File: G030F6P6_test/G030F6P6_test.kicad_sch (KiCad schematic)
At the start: 1 part

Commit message: Update G030F6P6_test.kicad_sch
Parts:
- added J?: Conn_01x10_Female, Connector_PinHeader_2.54mm:PinHeader_1x10_P2.54mm_Vertical, symbol Connector:Conn_01x10_Female
- added J?: (no value), symbol Connector:Conn_01x10_Female
- U?: value (none) -> STM32G030FxP; footprint (none) -> Package_SO:TSSOP-20_4.4x6.5mm_P0.65mm
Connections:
- net PIN1: now reaches U?.1 (PB7/PB8)
- net PIN1: now also J?.1 (Pin_1)
- net PIN10: now reaches U?.10 (PA3)
- net PIN10: now also J?.10 (Pin_10)
- net PIN11: now reaches U?.11 (PA4)
- net PIN11: now also J?.1 (Pin_1)
- net PIN12: now reaches U?.12 (PA5)
- net PIN12: now also J?.2 (Pin_2)
- net PIN13: now reaches U?.13 (PA6)
- net PIN13: now also J?.3 (Pin_3)
- net PIN14: now reaches U?.14 (PA7)
- net PIN14: now also J?.4 (Pin_4)
- net PIN15: now reaches U?.15 (PB0/PB1/PB2/PA8)
- net PIN15: now also J?.5 (Pin_5)
- net PIN16: now reaches U?.16 (PA11[PA9])
- net PIN16: now also J?.6 (Pin_6)
- net PIN17: now reaches U?.17 (PA12[PA10])
- net PIN17: now also J?.7 (Pin_7)
- net PIN18: now reaches U?.18 (PA13)
- net PIN18: now also J?.8 (Pin_8)
- net PIN19: now reaches U?.19 (PA15/PA14-BOOT0)
- net PIN19: now also J?.9 (Pin_9)
- net PIN2: now reaches U?.2 (PB9/PC14-OSC32_IN)
- net PIN2: now also J?.2 (Pin_2)
- net PIN20: now reaches U?.20 (PB3/PB4/PB5/PB6)
- net PIN20: now also J?.10 (Pin_10)
- net PIN3: now reaches U?.3 (PC15-OSC32_OUT)
- net PIN3: now also J?.3 (Pin_3)
- net PIN4: now reaches U?.4 (VDD/VDDA)
- net PIN4: now also J?.4 (Pin_4)
- net PIN5: now reaches U?.5 (VSS/VSSA)
- net PIN5: now also J?.5 (Pin_5)
- net PIN6: now reaches U?.6 (NRST)
- net PIN6: now also J?.6 (Pin_6)
- net PIN7: now reaches U?.7 (PA0)
- net PIN7: now also J?.7 (Pin_7)
- net PIN8: now reaches U?.8 (PA1)
- net PIN8: now also J?.8 (Pin_8)
- net PIN9: now reaches U?.9 (PA2)
- net PIN9: now also J?.9 (Pin_9)

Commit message: Update G030F6P6_test.kicad_sch
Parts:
- J1: renamed from J?; value (none) -> Conn_01x10_Female; footprint (none) -> Connector_PinHeader_2.54mm:PinHeader_1x10_P2.54mm_Vertical
- gave numbers to parts that had none: 2
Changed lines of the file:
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@@
   (symbol (lib_id "Connector:Conn_01x10_Female") (at 67.31 120.015 0) (unit 1)
     (in_bom yes) (on_board yes)
-    (property "Reference" "J?" (id 0) (at 63.5 106.045 0)
+    (property "Reference" "J2" (id 0) (at 63.5 106.045 0)
       (effects (font (size 1.27 1.27)) (justify left))
     )
@@
   (symbol (lib_id "MCU_ST_STM32G0:STM32G030FxP") (at 151.13 87.63 0) (unit 1)
     (in_bom yes) (on_board yes) (fields_autoplaced)
-    (property "Reference" "U?" (id 0) (at 139.065 66.04 0))
+    (property "Reference" "U1" (id 0) (at 139.065 66.04 0))
     (property "Value" "STM32G030FxP" (id 1) (at 139.065 68.58 0))
     (property "Footprint" "Package_SO:TSSOP-20_4.4x6.5mm_P0.65mm" (id 2) (at 181.61 121.92 0)
@@
   (symbol (lib_id "Connector:Conn_01x10_Female") (at 67.31 89.535 0) (unit 1)
     (in_bom yes) (on_board yes)
-    (property "Reference" "J?" (id 0) (at 63.5 75.565 0)
+    (property "Reference" "J1" (id 0) (at 63.5 75.565 0)
       (effects (font (size 1.27 1.27)) (justify left))
     )
-    (property "Value" "" (id 1) (at 69.215 92.0749 0)
+    (property "Value" "Conn_01x10_Female" (id 1) (at 69.215 92.0749 0)
       (effects (font (size 1.27 1.27)) (justify left) hide)
     )
-    (property "Footprint" "" (id 2) (at 67.31 89.535 0)
+    (property "Footprint" "Connector_PinHeader_2.54mm:PinHeader_1x10_P2.54mm_Vertical" (id 2) (at 67.31 89.535 0)
       (effects (font (size 1.27 1.27)) hide)
     )
@@
   )
   (symbol_instances
+    (path "/e9b753db-4772-4244-b88b-22e987cc4a07"
+      (reference "J1") (unit 1) (value "Conn_01x10_Female") (footprint "Connector_PinHeader_2.54mm:PinHeader_1x10_P2.54mm_Vertical")
+    )
     (path "/dea68bd7-448e-4645-961d-024e3f8df3a0"
-      (reference "J?") (unit 1) (value "Conn_01x10_Female") (footprint "Connector_PinHeader_2.54mm:PinHeader_1x10_P2.54mm_Vertical")
-    )
-    (path "/e9b753db-4772-4244-b88b-22e987cc4a07"
-      (reference "J?") (unit 1) (value "Conn_01x10_Female") (footprint "Connector_PinHeader_2.54mm:PinHeader_1x10_P2.54mm_Vertical")
+      (reference "J2") (unit 1) (value "Conn_01x10_Female") (footprint "Connector_PinHeader_2.54mm:PinHeader_1x10_P2.54mm_Vertical")
     )
     (path "/e65b62be-e01b-4688-a999-1d1be370c4ae"
-      (reference "U?") (unit 1) (value "STM32G030FxP") (footprint "Package_SO:TSSOP-20_4.4x6.5mm_P0.65mm")
+      (reference "U1") (unit 1) (value "STM32G030FxP") (footprint "Package_SO:TSSOP-20_4.4x6.5mm_P0.65mm")
     )
   )

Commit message: Update G030F6P6_test.kicad_sch
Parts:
- added C? (x4): 0.1uF, Capacitor_SMD:C_0805_2012Metric, symbol Device:C
- added D?: TX, LED_SMD:LED_0805_2012Metric, symbol Device:LED
- added D?: PWR, LED_SMD:LED_0805_2012Metric, symbol Device:LED
- added D?: RX, LED_SMD:LED_0805_2012Metric, symbol Device:LED
- added F?: Fuse, Fuse:Fuse_0805_2012Metric, symbol Device:Fuse
- added J?: USB_C_Receptacle_USB2.0, Connector_USB:USB_C_Receptacle_HRO_TYPE-C-31-M-12, symbol Connector:USB_C_Receptacle_USB2.0
- added JP? (x2): SolderJumper_2_Bridged, Jumper:SolderJumper-2_P1.3mm_Bridged2Bar_RoundedPad1.0x1.5mm, symbol Jumper:SolderJumper_2_Bridged
- added JP?: (no value), symbol Jumper:SolderJumper_2_Bridged
- added R? (x2): 1k, Resistor_SMD:R_0805_2012Metric, symbol Device:R
- added R?: 330, Resistor_SMD:R_0805_2012Metric, symbol Device:R
- added R? (x2): 5K1, Resistor_SMD:R_0805_2012Metric, symbol Device:R
- added U?: XC6206P332MR, Package_TO_SOT_SMD:SOT-23, symbol Regulator_Linear:XC6206PxxxMR
- added U?: CH340N, Package_SO:SOIC-8_3.9x4.9mm_P1.27mm, symbol Interface_USB:CH330N
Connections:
- new net: F?.1, J?.A4 (VBUS), J?.A9 (VBUS), J?.B4 (VBUS), J?.B9 (VBUS)
- new net: D?.2 (A), R?.1 (x3)
- new net +3V3: C?.1, U?.2 (VO)
- new net +5V: C?.1, F?.2, U?.3 (VI)
- new net 3V3: C?.1, U?.8 (V3)
- new net CC1: J?.A5 (CC1), R?.2
- new net CC2: J?.B5 (CC2), R?.2
- new net GND: C?.2, C?.2, C?.2, C?.2, D?.1 (K), J?.A1 (GND), J?.A12 (GND), J?.B1 (GND), J?.B12 (GND), J?.S1 (SHIELD), R?.1, R?.1, U?.1 (GND), U?.3 (GND)
- new net RXD: D?.1 (K), U?.7 (RXD)
- new net TXD: D?.1 (K), U?.6 (TXD)
- new net USBD+: J?.A6 (D+), J?.B6 (D+), U?.1 (UD+)
- new net USBD-: J?.A7 (D-), J?.B7 (D-), U?.2 (UD-)
- new net VCC: C?.1, R?.2, R?.2, R?.2, U?.5 (VCC)
- new net ~{RTS}: U?.4 (~{RTS})
- no-connect marks 0 -> 2
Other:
- note added: "CH340N USB-UART chip"
- note added: "LED"
- note added: "USB TYPE-C & Fuse"
- note added: "voltage regulator"
- moved on the sheet: J1, J2, U1

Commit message: add 元件
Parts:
- added J?: Conn_01x05_Female, Connector_PinHeader_2.54mm:PinHeader_1x05_P2.54mm_Vertical, symbol Connector:Conn_01x05_Female
- added JP? (x3): SolderJumper_2_Bridged, Jumper:SolderJumper-2_P1.3mm_Bridged2Bar_RoundedPad1.0x1.5mm, symbol Jumper:SolderJumper_2_Bridged
- added R?: (no value), symbol Device:R
- JP?: value (none) -> SolderJumper_2_Bridged; footprint (none) -> Jumper:SolderJumper-2_P1.3mm_Bridged2Bar_RoundedPad1.0x1.5mm
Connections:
- net +3V3: now also J?.1 (Pin_1)
- net GND: now also J?.2 (Pin_2), R?.1
- net PIN1: now also JP?.2 (B)
- net PIN19: now also JP?.2 (B), R?.2
- net PIN20: now also JP?.2 (B)
- net RXD: now also JP?.1 (A)
- net TXD: now also JP?.1 (A)
- net ~{RTS}: now also JP?.1 (A)
- new net NRST: J?.5 (Pin_5)
- new net SWCLK: J?.4 (Pin_4)
- new net SWDIO: J?.3 (Pin_3)
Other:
- note added: "SWD connect"
- moved on the sheet: JP?

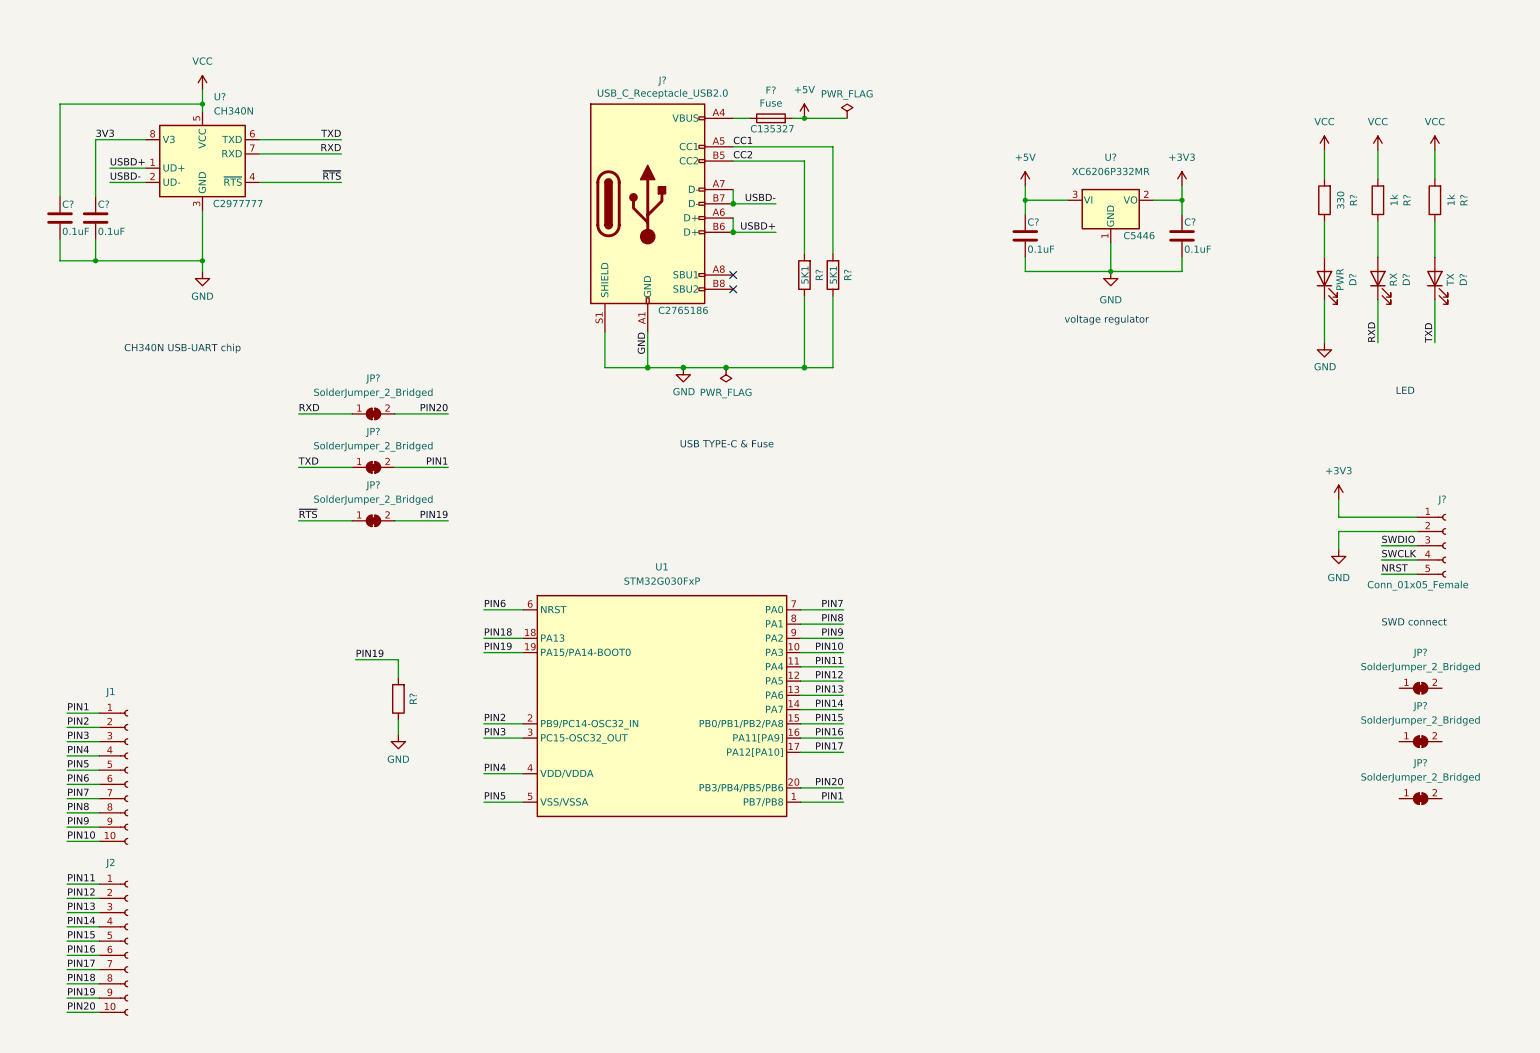
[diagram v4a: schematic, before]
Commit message: Update G030F6P6_test.kicad_sch
移除jump 的 BOM 標記
新增CH343P 元件
連結各對外腳位(SWD、UART、BOOT0)
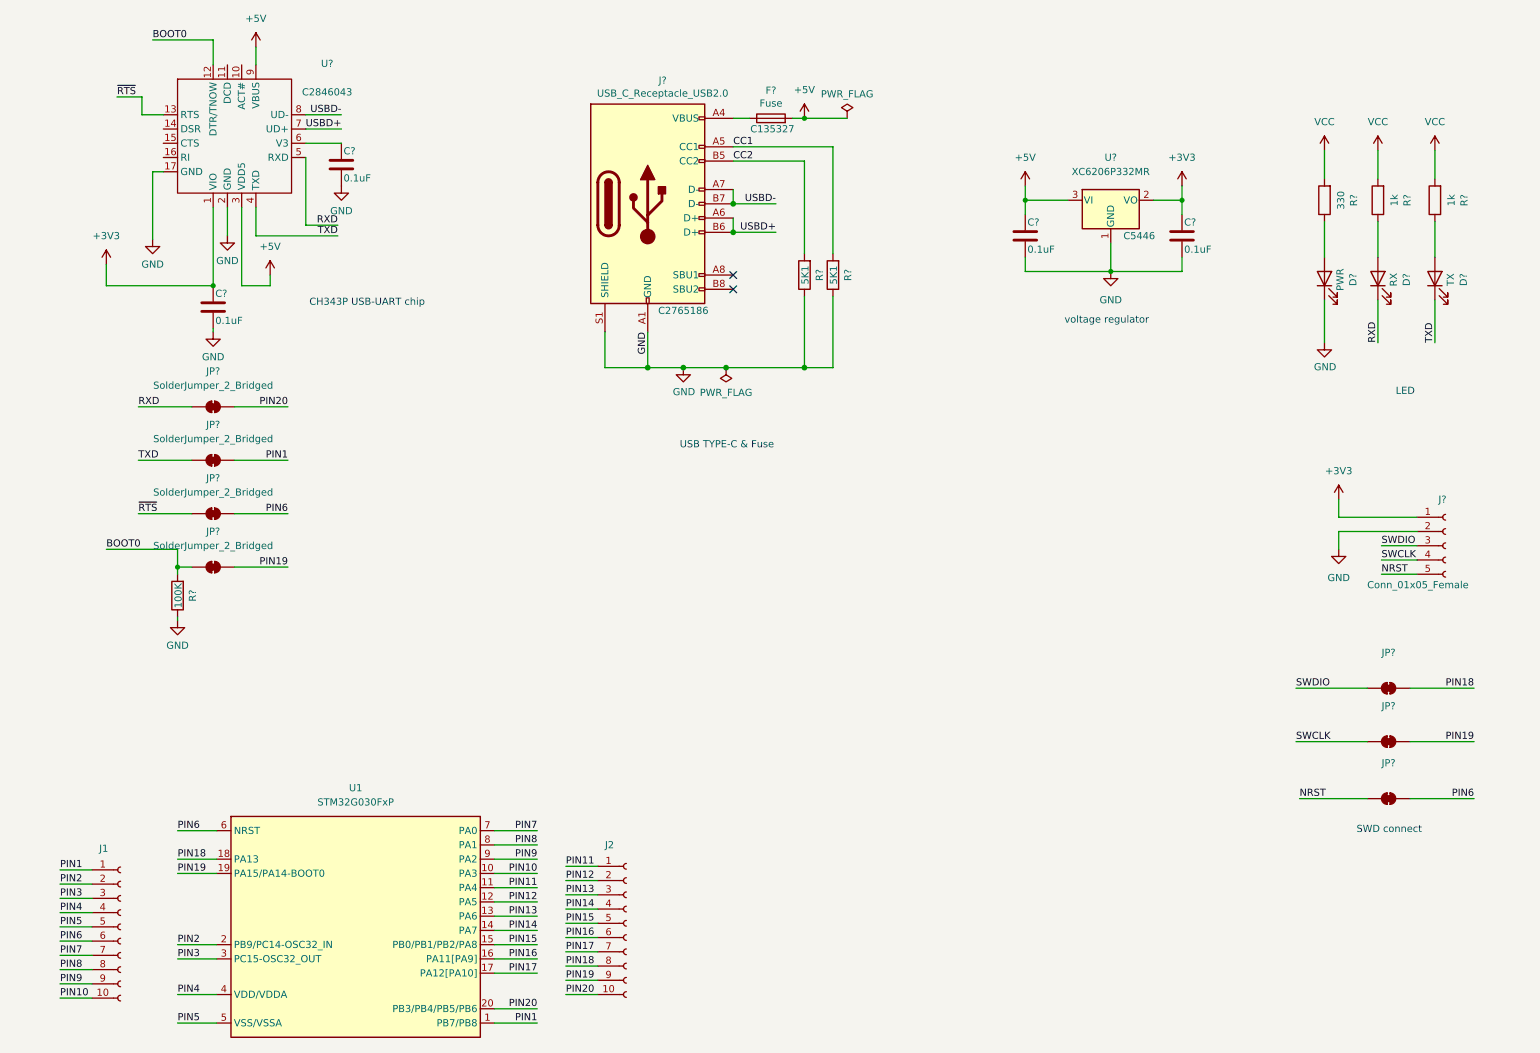
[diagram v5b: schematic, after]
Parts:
- removed JP? (x3): SolderJumper_2_Bridged, Jumper:SolderJumper-2_P1.3mm_Bridged2Bar_RoundedPad1.0x1.5mm, symbol Jumper:SolderJumper_2_Bridged
- removed U?: CH340N, Package_SO:SOIC-8_3.9x4.9mm_P1.27mm, symbol Interface_USB:CH330N
- added JP? (x4): SolderJumper_2_Bridged, Jumper:SolderJumper-2_P1.3mm_Bridged2Bar_RoundedPad1.0x1.5mm, symbol Jumper:SolderJumper_2_Bridged
- added U?: (no value), symbol Interface_USB:CH343P
- JP? (x3): value SolderJumper_2_Bridged -> (none); footprint Jumper:SolderJumper-2_P1.3mm_Bridged2Bar_RoundedPad1.0x1.5mm -> (none); now left out of the parts list
- R?: value (none) -> 100K; footprint (none) -> Resistor_SMD:R_0805_2012Metric
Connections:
- net +3V3: now also C?.1, U?.1 (VIO)
- net +5V: now also U?.3 (VDD5), U?.9 (VBUS)
- net GND: now also U?.17 (GND), U?.2 (GND)
- net NRST: now also JP?.1 (A)
- net PIN1: now also JP?.2 (B)
- net PIN18: now also JP?.2 (B)
- net PIN19: now also JP?.2 (B), JP?.2 (B); no longer R?.2
- net PIN20: now also JP?.2 (B)
- net PIN6: now also JP?.2 (B), JP?.2 (B)
- net RXD: now also JP?.1 (A), U?.5 (RXD)
- net SWCLK: now also JP?.1 (A)
- net SWDIO: now also JP?.1 (A)
- net TXD: now also JP?.1 (A), U?.4 (TXD)
- net USBD+: now also U?.7 (UD+)
- net USBD-: now also U?.8 (UD-)
- net VCC: no longer C?.1
- net ~{RTS}: now also JP?.1 (A), U?.13 (RTS)
- net 3V3: no longer names the net of C?.1
- net 3V3: now also U?.6 (V3)
- new net BOOT0: JP?.1 (A), R?.2, U?.12 (DTR/TNOW)
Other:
- note added: "CH343P USB-UART chip"
- note removed: "CH340N USB-UART chip"
- moved on the sheet: C?, J1, J2, R?, U1

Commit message: Update G030F6P6_test.kicad_sch
增加 VBUS、外部電源選擇接腳
執行電器檢查正常規則調整
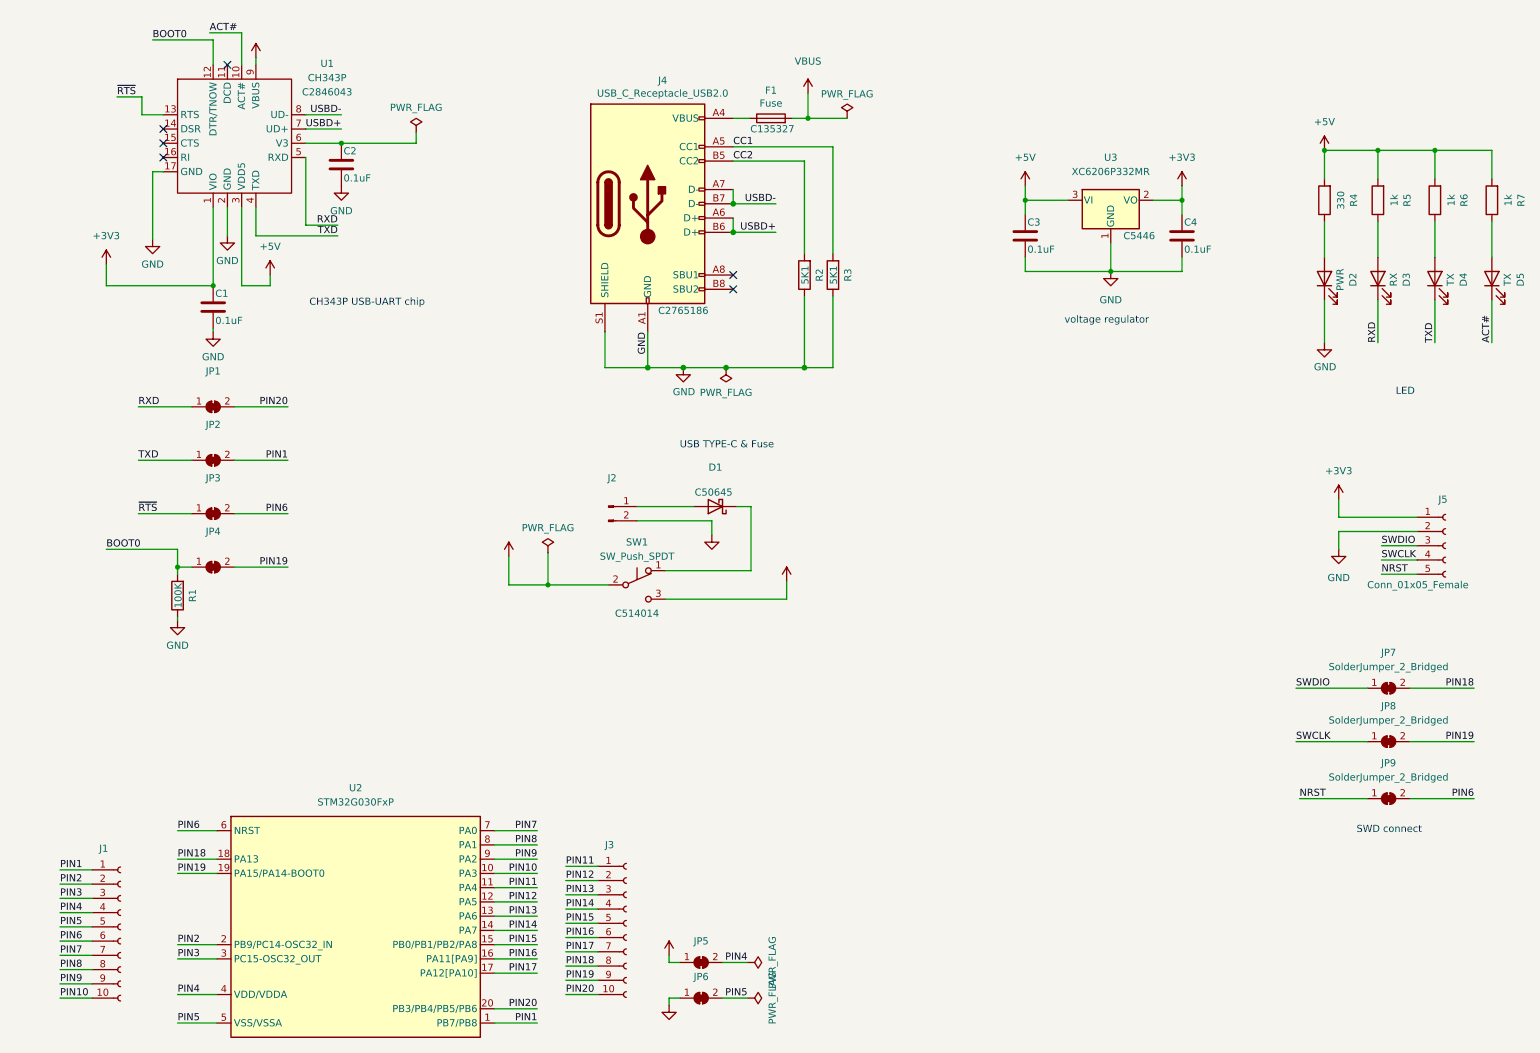
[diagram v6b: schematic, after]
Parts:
- added D1: (no value), symbol Device:D_Schottky
- added D5: TX, LED_SMD:LED_0805_2012Metric, symbol Device:LED
- added J2: (no value), symbol Connector:Conn_01x02_Male
- added JP5, JP6: (no value), symbol Jumper:SolderJumper_2_Bridged
- added R7: 1k, Resistor_SMD:R_0805_2012Metric, symbol Device:R
- added SW1: SW_Push_SPDT, Button_Switch_SMD:SW_SPDT_PCM12, symbol Switch:SW_Push_SPDT
- JP1, JP2, JP3, JP4: renamed from JP?; value SolderJumper_2_Bridged -> (none); footprint Jumper:SolderJumper-2_P1.3mm_Bridged2Bar_RoundedPad1.0x1.5mm -> (none)
- JP7, JP8, JP9: renamed from JP?; value (none) -> SolderJumper_2_Bridged; footprint (none) -> Jumper:SolderJumper-2_P1.3mm_Bridged2Bar_RoundedPad1.0x1.5mm
- U1: renamed from U?; value (none) -> CH343P; footprint (none) -> Package_DFN_QFN:QFN-16-1EP_3x3mm_P0.5mm_EP1.45x1.45mm
- gave numbers to parts that had none: 17
- renumbered J2 to J3, U1 to U2
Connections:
- net VCC is gone; now on net +5V: R4.2, R5.2, R6.2
- net +5V: now also JP5.1 (A), R7.2, SW1.2 (B); no longer F1.2, U1.9 (VBUS)
- net GND: now also J2.2 (Pin_2), JP6.1 (A)
- net PIN4: now also JP5.2 (B)
- net PIN5: now also JP6.2 (B)
- net ACT#: now reaches U1.10 (ACT#)
- net ACT#: now also D5.1 (K)
- new net: D1.1 (K), SW1.1 (A)
- new net: D1.2 (A), J2.1 (Pin_1)
- new net: D5.2 (A), R7.1
- new net VBUS: F1.2, SW1.3 (C), U1.9 (VBUS)
- no-connect marks 2 -> 6
